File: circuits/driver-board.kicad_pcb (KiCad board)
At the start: 2 copper layers, 40 x 47 mm, 54 parts, among them J1 Backpack_Conn_02x09, J2 USB4120-03-C_REVA, J3 Motor_Conn_01x04, Q1 MMBT3904, Q2 MMBT3904, SW1 ESP_EN_SW_Push, SW2 ESP_IO0_SW_Push, U1 CP2102N-A01-GQFN24, U2 BAxxXX0, U3 ESP32-S3, U4 AS5601-ASOT, U5 TMC2209-LA, U6 STUSB4500QTR

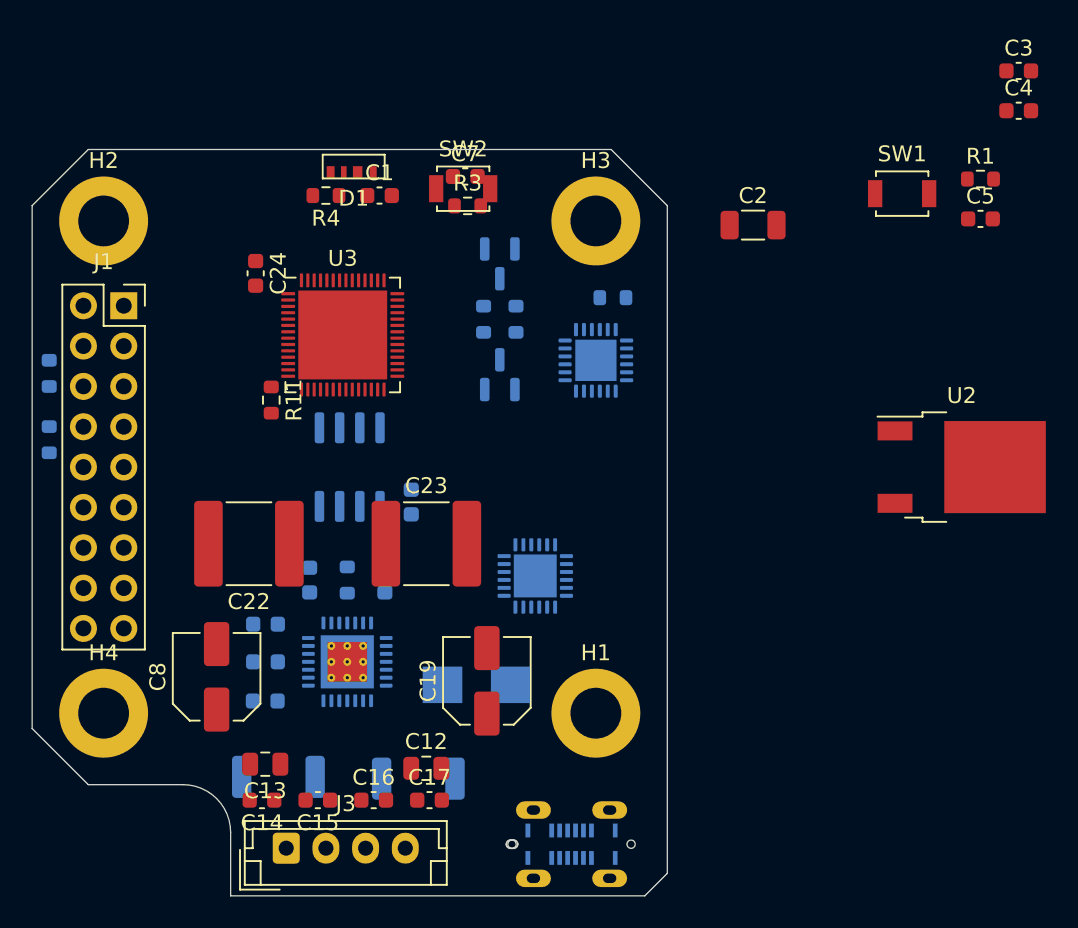
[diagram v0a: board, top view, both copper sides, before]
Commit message: work on external spram and pcb layout
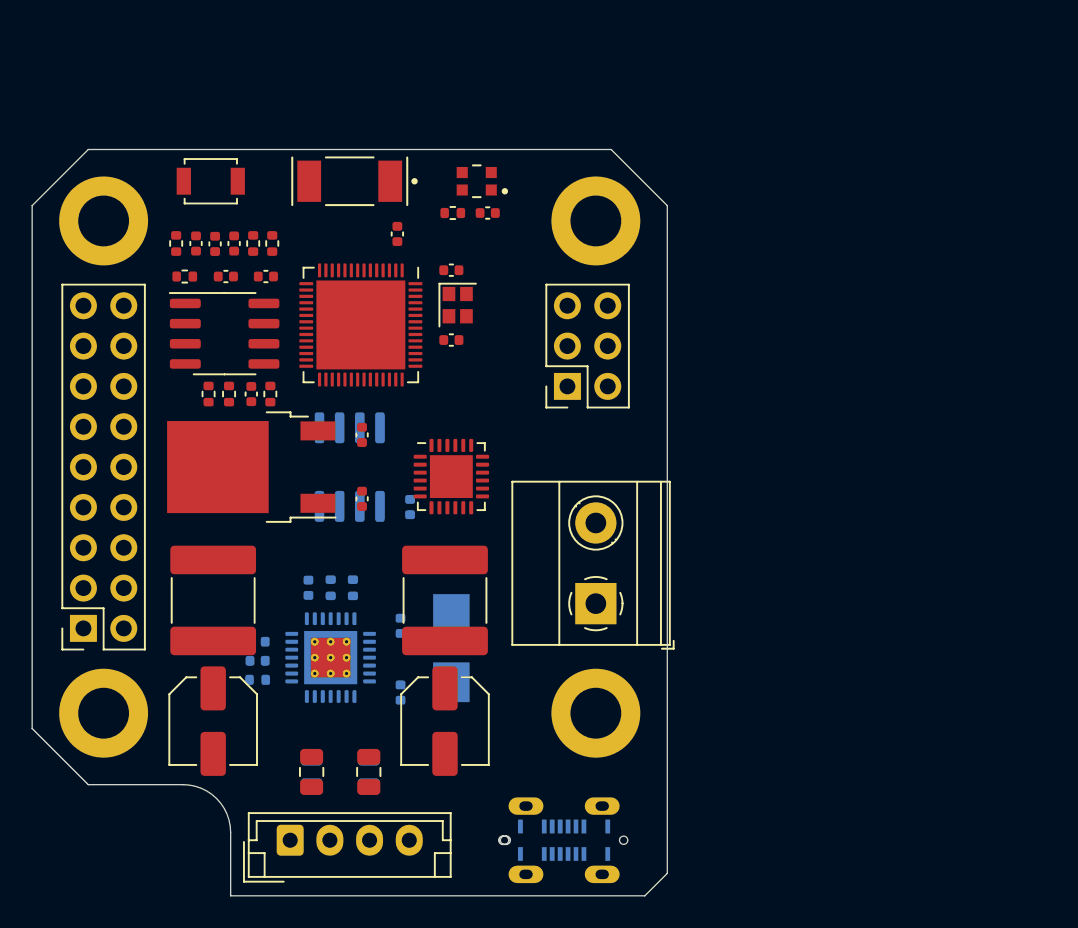
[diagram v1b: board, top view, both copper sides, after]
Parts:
- removed C14, C15, C16, C17: 100nF-100V, Capacitor_SMD:C_0603_1608Metric
- removed C7: 2µ2F-6.3V, Capacitor_SMD:C_0603_1608Metric
- removed Q1, Q2: MMBT3904, Package_TO_SOT_SMD:SOT-23
- removed R15: 10K-0402, Resistor_SMD:R_0603_1608Metric
- removed R16, R17: 10K-0603, Resistor_SMD:R_0603_1608Metric
- removed R3: 4K7-0402, Resistor_SMD:R_0603_1608Metric
- removed SW2: ESP_IO0_SW_Push, Button_Switch_SMD:SW_SPST_B3U-1000P
- removed U1: CP2102N-A01-GQFN24, Package_DFN_QFN:QFN-24-1EP_4x4mm_P0.5mm_EP2.6x2.6mm
- added AE1: Antenna, Slimc_RF_Antenna:XCVR_NN01-102, F.Cu at (100.0, 82.0)
- added C20: TBD, Capacitor_SMD:C_0402_1005Metric, F.Cu at (103.0, 85.3)
- added C25: 1µF-6v3, Capacitor_SMD:C_0402_1005Metric, F.Cu at (106.4, 87.6)
- added C26: 1µF-6v3, Capacitor_SMD:C_0402_1005Metric, F.Cu at (106.4, 92.0)
- added C27: 1µF-6v3, Capacitor_SMD:C_0402_1005Metric, F.Cu at (93.8, 95.4)
- added C28: 1µF-6v3, Capacitor_SMD:C_0402_1005Metric, F.Cu at (94.7, 88.0)
- added C29: 0.1µF-6v3, Capacitor_SMD:C_0402_1005Metric, F.Cu at (92.2, 88.0)
- added J4: Screw_Terminal_01x02, TerminalBlock_Phoenix:TerminalBlock_Phoenix_MKDS-1,5-2-5.08_1x02_P5.08mm_Horizontal, F.Cu at (115.5, 108.6)
- added J5: Conn_01x06_Female, Connector_PinSocket_2.54mm:PinSocket_2x03_P2.54mm_Vertical, F.Cu at (113.7, 94.9)
- added R14: 4K7-0402, Resistor_SMD:R_0402_1005Metric, F.Cu at (95.0, 95.4)
- added R2: 20K-0402, Resistor_SMD:R_0402_1005Metric, B.Cu at (98.8, 107.6)
- added R5: 715K-0402, Resistor_SMD:R_0402_1005Metric, F.Cu at (92.4, 95.4)
- added R6: 110K-0402, Resistor_SMD:R_0402_1005Metric, F.Cu at (91.1, 95.4)
- added R9: 100K-0402, Resistor_SMD:R_0402_1005Metric, F.Cu at (89.6, 88.0)
- added U7: ESP-PSRAM32, Package_SO:SOIC-8_3.9x4.9mm_P1.27mm, F.Cu at (92.1, 91.6)
- added Y1: 40Mhz, Crystal:Crystal_SMD_2016-4Pin_2.0x1.6mm, F.Cu at (106.8, 89.8)
- C1: value 100nF-6.3V-0603 -> 100nF-6v3-0603; footprint Capacitor_SMD:C_0603_1608Metric -> Capacitor_SMD:C_0402_1005Metric
- C10, C11, C18, C21: footprint Capacitor_SMD:C_0603_1608Metric -> Capacitor_SMD:C_0402_1005Metric
- C2: value ??µF 35V -> 1µF-6v3; footprint Capacitor_SMD:C_1206_3216Metric -> Capacitor_SMD:C_0402_1005Metric
- C24: value 100µF-6.3V-0603 -> 1µF-6v3; footprint Capacitor_SMD:C_0603_1608Metric -> Capacitor_SMD:C_0402_1005Metric
- C3: value ??µF-0603 -> 10µF-35V-0603; footprint Capacitor_SMD:C_0603_1608Metric -> Capacitor_SMD:C_0402_1005Metric
- C4: value 10µF-0603 -> 1µF-6v3-0603; footprint Capacitor_SMD:C_0603_1608Metric -> Capacitor_SMD:C_0402_1005Metric
- C5: value 2µ2F-6.3V -> 0.1µF-6v3; footprint Capacitor_SMD:C_0603_1608Metric -> Capacitor_SMD:C_0402_1005Metric
- C6: value 100nF -> 100nF-6v3-0603; footprint Capacitor_SMD:C_0603_1608Metric -> Capacitor_SMD:C_0402_1005Metric
- C9: value 2µ2F-6.3V -> 2µ2F-6v3; footprint Capacitor_SMD:C_0603_1608Metric -> Capacitor_SMD:C_0402_1005Metric
- D1: footprint Slimc_LED_SMD:WS2812_4020_SIDE -> Slimc_LED_SMD:LED_WS2812C-2020
- J1: value Backpack_Conn_02x09 -> Conn_01x18_Female
- R1: value 4K7-0402 -> 10K-0402; footprint Resistor_SMD:R_0603_1608Metric -> Resistor_SMD:R_0402_1005Metric
- R10, R8: footprint Resistor_SMD:R_0603_1608Metric -> Resistor_SMD:R_0402_1005Metric; moved to F.Cu
- R11: footprint Resistor_SMD:R_0603_1608Metric -> Resistor_SMD:R_0402_1005Metric; moved to B.Cu
- R12, R13: value 0R11-2010-1W -> 0R11-0805-1W; footprint Resistor_SMD:R_2010_5025Metric -> Resistor_SMD:R_0805_2012Metric
- R4, R7: footprint Resistor_SMD:R_0603_1608Metric -> Resistor_SMD:R_0402_1005Metric
- SW1: value ESP_EN_SW_Push -> RST_SW_Push
- U2: value BAxxXX0 -> BA33DD0T
- U6: moved to F.Cu
- moved R1 50.8 mm to (89.1, 85.9), turned to 90 degrees
- moved C3 49.4 mm to (100.8, 102.0), turned to -90 degrees
- moved C5 48.2 mm to (91.5, 85.9), turned to -90 degrees
- moved C4 46.1 mm to (100.8, 98.0), turned to 90 degrees
- moved U2 44.7 mm to (93.8, 100.0), turned to 180 degrees
- moved SW1 43.5 mm to (91.2, 82.0)
- moved C2 35.1 mm to (90.3, 85.9), turned to -90 degrees
- moved J1 20.5 mm to (83.2, 110.2), turned to 180 degrees
- moved R10 18.7 mm to (95.1, 85.9)
- moved R8 15.2 mm to (93.9, 85.9), turned to 90 degrees
- moved C23 13.9 mm to (91.4, 108.4), turned to 90 degrees
- moved R11 12.9 mm to (100.2, 107.6)
- moved C22 12.9 mm to (106.0, 108.4), turned to 90 degrees
- moved C21 8.54 mm to (103.2, 114.2), turned to 90 degrees
- moved R7 8.45 mm to (94.2, 113.4), turned to 180 degrees
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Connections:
- C2 pad 1: VBUS -> ESP_EN
- C24 pad 1: +3V3 -> GND
- C24 pad 2: GND -> +3V3
- C5 pad 1: ESP_EN -> GND
- C5 pad 2: GND -> +3V3
- C6 pad 1: +3V3 -> GND
- C6 pad 2: GND -> +3V3
- C9 pad 1: GND -> Net-(C9-Pad1)
- C9 pad 2: Net-(C9-Pad2) -> GND
- J1 pad 10: ESP_IO19 -> ESP_IO18
- J1 pad 11: ESP_IO18 -> ESP_IO17
- J1 pad 12: ESP_IO12 -> ESP_IO14
- J1 pad 13: ESP_IO05 -> GND
- J1 pad 14: ESP_IO04 -> ESP_IO06
- J1 pad 15: SVN -> ESP_IO05
- J1 pad 16: SVP -> ESP_IO04
- J1 pad 17: VBUS -> ESP_IO46
- J1 pad 18: GND -> ESP_IO45
- J1 pad 2: +3V3 -> VBUS
- J1 pad 3: ESP_IO00 -> GND
- J1 pad 4: ESP_EN -> VBUS
- J1 pad 5: AS5601_ABI_A -> GND
- J1 pad 6: AS5601_ABI_A -> VBUS
- J1 pad 7: AS5601_ABI_A -> unconnected-(J1-Pad7)
- J1 pad 8: AS5601_ABI_A -> unconnected-(J1-Pad8)
- J1 pad 9: ESP_IO26 -> ESP_IO19
- R1 pad 1: ESP_EN -> +3V3
- R1 pad 2: +3V3 -> ESP_EN
- R10 pad 2: AS5601_ABI_A -> ESP_IO04
- R11 pad 1: AS5601_ABI_A -> ESP_IO45
- R11 pad 2: AS5601_ABI_A -> ESP_IO46
- R7 pad 1: +3V3 -> ESP_IO06
- R7 pad 2: AS5601_ABI_A -> +3V3
- R8 pad 2: AS5601_ABI_A -> ESP_IO05
- SW1 pad 1: ESP_EN -> GND
- SW1 pad 2: GND -> ESP_EN
- U2 pad 2: Net-(U2-Pad2) -> GND
- U3 pad 15: ESP_IO10 -> AS5601_ABI_A
- U3 pad 16: ESP_IO11 -> AS5601_ABI_B
- U3 pad 28: unconnected-(U3-Pad28) -> ESP_SPICS1
- U3 pad 29: unconnected-(U3-Pad29) -> ESP_SPIVDD
- U3 pad 30: unconnected-(U3-Pad30) -> ESP_SPIHD
- U3 pad 31: unconnected-(U3-Pad31) -> ESP_SPIWP
- U3 pad 33: unconnected-(U3-Pad33) -> ESP_SPICLK
- U3 pad 34: unconnected-(U3-Pad34) -> ESP_SPIQ
- U3 pad 35: unconnected-(U3-Pad35) -> ESP_SPID
- U3 pad 37: unconnected-(U3-Pad37) -> Net-(C27-Pad2)
- U3 pad 52: ESP_IO00 -> ESP_IO46
- U3 pad 53: unconnected-(U3-Pad53) -> Net-(C26-Pad2)
- U3 pad 54: unconnected-(U3-Pad54) -> Net-(C25-Pad2)
- U4 pad 5: AS5601_ABI_A -> AS5601_ABI_B
- U4 pad 6: AS5601_ABI_A -> ESP_IO05
- U4 pad 7: AS5601_ABI_A -> ESP_IO04
- U5 pad 11: AS5601_ABI_A -> ESP_IO07
- U5 pad 14: AS5601_ABI_A -> ESP_IO46
- U5 pad 16: AS5601_ABI_A -> ESP_IO08
- U5 pad 19: AS5601_ABI_A -> ESP_IO09
- U5 pad 2: AS5601_ABI_A -> ESP_IO06
- U5 pad 8: Net-(C9-Pad2) -> Net-(C9-Pad1)
- U6 pad 7: AS5601_ABI_A -> ESP_IO04
- U6 pad 8: AS5601_ABI_A -> ESP_IO05

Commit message: couple of renders
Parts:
- moved C23 70.7 mm to (41.4, 58.4)
- moved D3 70.7 mm to (56.4, 61.4)
- moved R5 70.7 mm to (42.4, 45.4)
- moved AE1 70.7 mm to (50.0, 32.0)
- moved C1 70.7 mm to (58.7, 34.0)
- moved C10 70.7 mm to (44.2, 61.0)
- moved C11 70.7 mm to (44.2, 62.2)
- moved C12 70.7 mm to (51.2, 69.2)
- moved C18 70.7 mm to (53.2, 60.0)
- moved C19 70.7 mm to (56.0, 66.0)
- moved C21 70.7 mm to (53.2, 64.2)
- moved C22 70.7 mm to (56.0, 58.4)
- moved C24 70.7 mm to (42.7, 35.9)
- moved C25 70.7 mm to (56.4, 37.6)
- moved C26 70.7 mm to (56.4, 42.0)
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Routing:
- added copper zone on B.Cu, net GND
- added copper zone on F.Cu, net GND

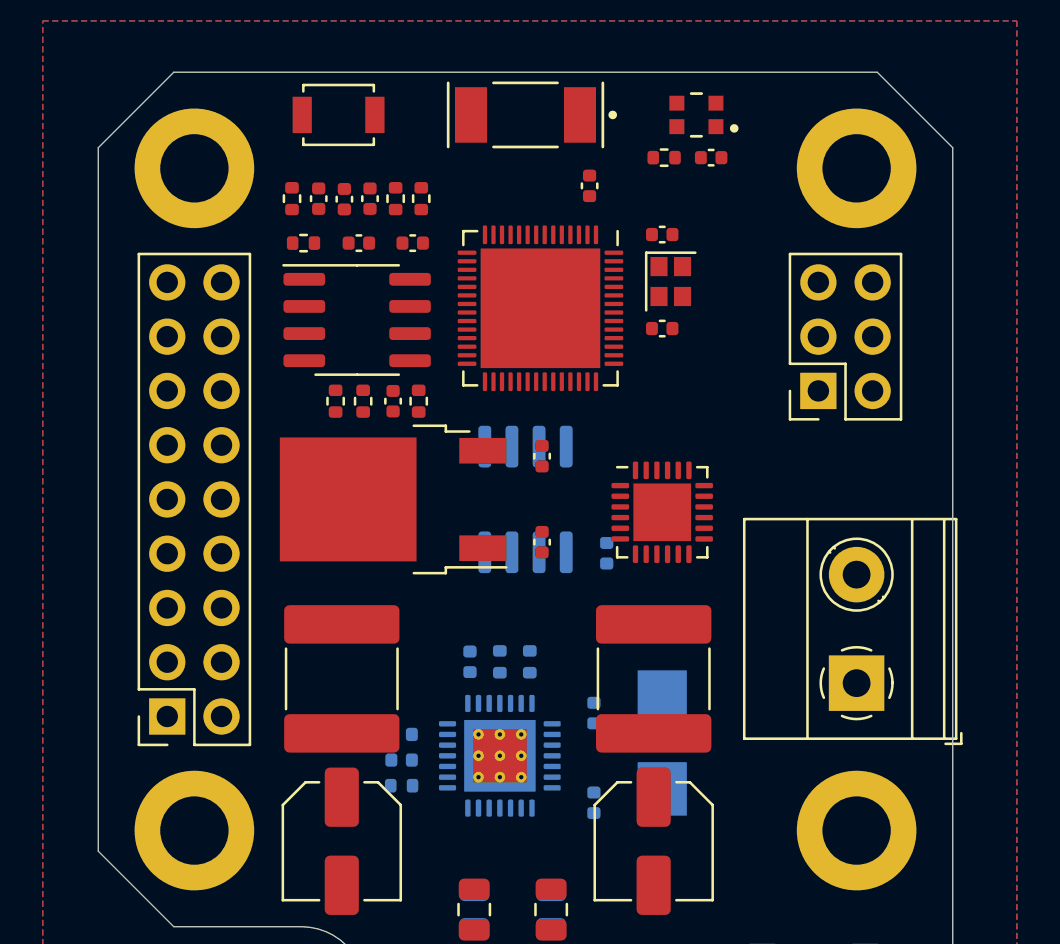
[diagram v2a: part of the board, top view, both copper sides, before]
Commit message: adjusting schematic and pcb component placement
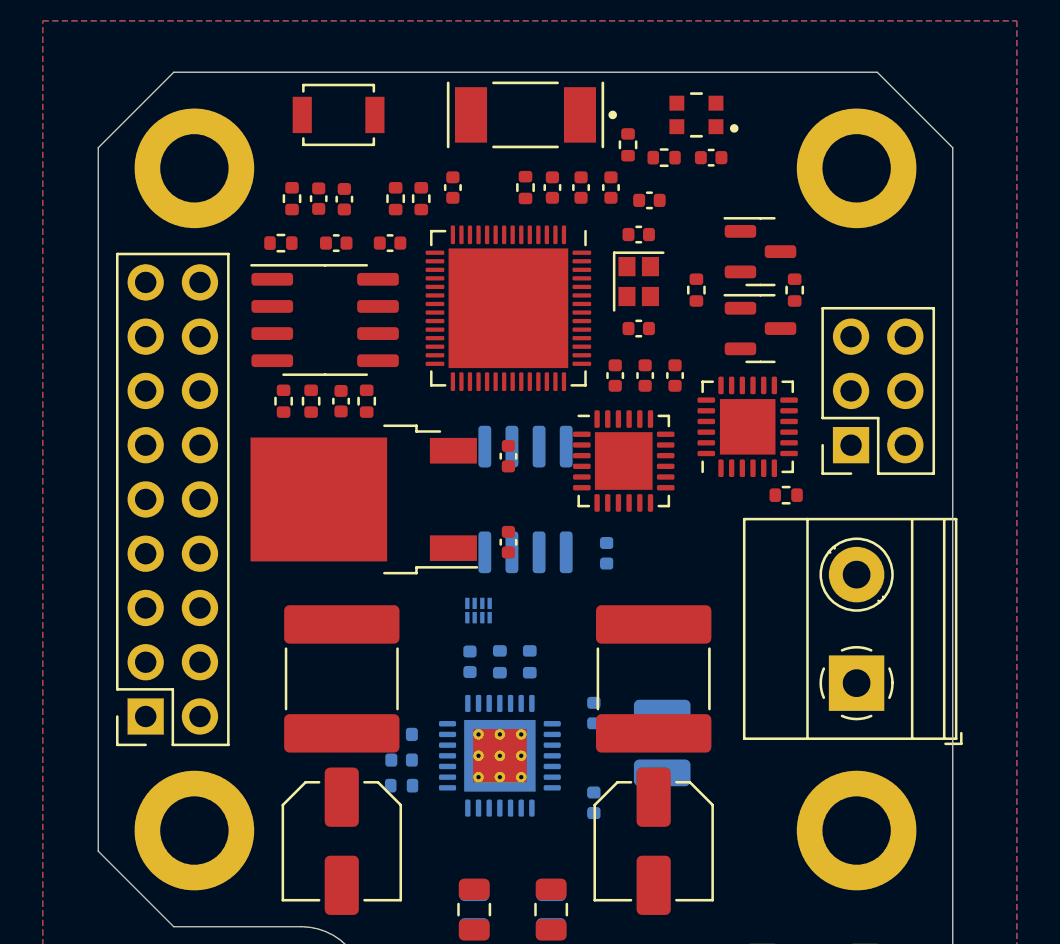
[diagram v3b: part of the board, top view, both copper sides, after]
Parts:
- removed C24: 1µF-6v3, Capacitor_SMD:C_0402_1005Metric
- added C30: 1µF, Capacitor_SMD:C_0402_1005Metric, F.Cu at (55.6, 44.2)
- added C31: 100nF, Capacitor_SMD:C_0402_1005Metric, F.Cu at (52.6, 35.4)
- added C32: 100nF, Capacitor_SMD:C_0402_1005Metric, F.Cu at (51.3, 35.4)
- added C33: 100nF, Capacitor_SMD:C_0402_1005Metric, F.Cu at (54.2, 44.2)
- added C34: 1pF, Capacitor_SMD:C_0402_1005Metric, F.Cu at (46.6, 35.4)
- added C35: 15pF, Capacitor_SMD:C_0402_1005Metric, F.Cu at (55.3, 37.6)
- added C7: 10nF, Capacitor_SMD:C_0402_1005Metric, F.Cu at (57.0, 44.2)
- added L1: 0R, Resistor_SMD:R_0402_1005Metric, F.Cu at (54.8, 33.4)
- added Q1: SS8050-G, Package_TO_SOT_SMD:SOT-23, F.Cu at (61.0, 38.4)
- added Q2: SS8050-G, Package_TO_SOT_SMD:SOT-23, F.Cu at (61.0, 42.0)
- added R15: 10K, Resistor_SMD:R_0402_1005Metric, F.Cu at (62.2, 49.8)
- added R16: 10K, Resistor_SMD:R_0402_1005Metric, F.Cu at (62.6, 40.2)
- added R17: 10K, Resistor_SMD:R_0402_1005Metric, F.Cu at (58.0, 40.2)
- added R3: 20K, Resistor_SMD:R_0402_1005Metric, F.Cu at (50.0, 35.4)
- added U1: CP2102N-A01-GQFN24, Package_DFN_QFN:QFN-24-1EP_4x4mm_P0.5mm_EP2.6x2.6mm, F.Cu at (60.4, 46.6)
- added U8: 74LVC2G00, Package_SON:X2SON-8_1.4x1mm_P0.35mm, B.Cu at (47.8, 55.2)
- C1, C6: value 100nF-6v3-0603 -> 100nF
- C12, C13: value 100nF-16V -> 100nF
- C18: value 100nF-25V -> 100nF
- C2, C27, C28: value 1µF-6v3 -> 1µF
- C20: value TBD -> NC
- C21: value 100nF-50V-0603 -> 100nF-50V
- C22, C23: value 10µF-50V-2220 -> 10µF-50V
- C25: value 1µF-6v3 -> 10µF
- C26: value 1µF-6v3 -> 15pF
- C29: value 0.1µF-6v3 -> 100nF
- C3: value 10µF-35V-0603 -> 10µF-35V
- C4: value 1µF-6v3-0603 -> 1µF
- C5: value 0.1µF-6v3 -> 1µF
- D3: value SMB28A -> SMB24A; footprint Diode_SMD:D_SMB -> Diode_SMD:D_1210_3225Metric
- J4: value Screw_Terminal_01x02 -> Screw_Terminals
- R1: value 10K-0402 -> 10K
- R10, R14, R8: value 4K7-0402 -> 4K7
- R11: value 1K-1%-0603 -> 1K-1%
- R2, R7: value 20K-0402 -> 20K
- R4: value 230R-0402 -> 230
- R5: value 715K-0402 -> 715K
- R6: value 110K-0402 -> 110K
- R9: value 100K-0402 -> 100K
- Y1: value 40Mhz -> 40MHz
- moved U6 3.00 mm to (54.6, 48.2)
- moved J5 2.97 mm to (65.2, 47.5)
- moved R14 2.44 mm to (42.6, 45.4)
- moved R6 2.44 mm to (38.7, 45.4)
- moved C27 2.43 mm to (41.4, 45.4)
- moved R5 2.43 mm to (40.0, 45.4)
- moved C25 1.71 mm to (55.8, 36.0)
- moved C3 1.57 mm to (49.2, 52.0)
- moved C4 1.57 mm to (49.2, 48.0)
- moved U3 1.50 mm to (49.2, 41.0)
- moved U7 1.50 mm to (40.6, 41.6)
- moved Y1 1.50 mm to (55.3, 39.8)
- moved U2 1.38 mm to (42.4, 50.0)
- moved C26 1.10 mm to (55.3, 42.0), turned to 180 degrees
- moved C28 1.06 mm to (43.7, 38.0)
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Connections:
- net Net-(C26-Pad2) renamed ESP_XTAL_N
- AE1 pad 1: Net-(AE1-Pad1) -> Net-(L1-Pad1)
- AE1 pad 2: (no net) -> GND
- C20 pad 1: Net-(AE1-Pad1) -> Net-(U3-Pad1)
- C20 pad 2: Net-(C20-Pad2) -> GND
- C25 pad 2: Net-(C25-Pad2) -> +3V3
- J1 pad 7: unconnected-(J1-Pad7) -> ESP_IO03
- J1 pad 8: unconnected-(J1-Pad8) -> ESP_IO02
- R2 pad 1: ESP_IO07 -> TMC2209_DIAG
- R4 pad 1: ESP_IO48 -> ESP_IO01
- U3 pad 1: Net-(C20-Pad2) -> Net-(U3-Pad1)
- U3 pad 15: AS5601_ABI_A -> ESP_IO10
- U3 pad 16: AS5601_ABI_B -> AS5601_ABI_A
- U3 pad 17: ESP_IO12 -> AS5601_ABI_B
- U3 pad 21: ESP_IO15 -> unconnected-(U3-Pad21)
- U3 pad 22: ESP_IO16 -> unconnected-(U3-Pad22)
- U3 pad 25: ESP_IO19 -> USB_D-
- U3 pad 26: ESP_IO20 -> USB_D+
- U3 pad 38: ESP_IO33 -> unconnected-(U3-Pad38)
- U3 pad 39: ESP_IO34 -> unconnected-(U3-Pad39)
- U3 pad 40: ESP_IO35 -> unconnected-(U3-Pad40)
- U3 pad 41: ESP_IO36 -> unconnected-(U3-Pad41)
- U3 pad 42: ESP_IO37 -> unconnected-(U3-Pad42)
- U3 pad 43: ESP_IO38 -> unconnected-(U3-Pad43)
- U3 pad 44: ESP_IO39 -> unconnected-(U3-Pad44)
- U3 pad 45: ESP_IO40 -> unconnected-(U3-Pad45)
- U3 pad 47: ESP_IO41 -> unconnected-(U3-Pad47)
- U3 pad 48: ESP_IO42 -> unconnected-(U3-Pad48)
- U3 pad 50: ESP_IO44 -> unconnected-(U3-Pad50)
- U3 pad 54: Net-(C25-Pad2) -> ESP_XTAL_P
- U5 pad 11: ESP_IO07 -> TMC2209_DIAG
- U5 pad 16: ESP_IO08 -> ESP_IO07
- U5 pad 19: ESP_IO09 -> ESP_IO08
- Y1 pad 1: Net-(C25-Pad2) -> ESP_XTAL_P
- Y1 pad 4: (no net) -> GND

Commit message: tmc2209 -> tmc 2226
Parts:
- C10, C11, C18, C21, C9, D3, R11, R12, R13, R2, R7, U8: moved to F.Cu
- U5: footprint Package_DFN_QFN:QFN-28-1EP_5x5mm_P0.5mm_EP3.35x3.35mm_ThermalVias -> Package_SO:HTSSOP-28-1EP_4.4x9.7mm_P0.65mm_EP3.4x9.5mm_ThermalVias; moved to F.Cu
- moved C10 9.40 mm to (53.6, 61.0), turned to 180 degrees
- moved C11 9.40 mm to (53.6, 62.2), turned to 180 degrees
- moved R7 9.40 mm to (53.6, 63.4), turned to 0 degrees
- moved D3 8.62 mm to (57.0, 52.8), turned to 180 degrees
- moved C18 8.60 mm to (44.6, 60.0)
- moved C21 8.60 mm to (44.6, 64.2)
- moved C9 3.00 mm to (50.4, 57.6)
- moved R11 2.60 mm to (47.6, 57.6)
- moved C13 2.20 mm to (45.4, 69.2)
- moved R12 1.40 mm to (49.8, 69.2)
- moved C12 0.80 mm to (52.0, 69.2)
- moved U5 0.32 mm to (48.8, 61.7), turned to 180 degrees
- moved R2 0.20 mm to (49.0, 57.6)
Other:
- copper layers 2 -> 4
